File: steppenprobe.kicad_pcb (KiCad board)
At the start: 2 copper layers, 50 x 60 mm, 75 parts, among them J1 USB_C_Receptacle_USB2.0, J2 Conn_01x12, U1 SRV05-4, U2 XC6206PxxxMR, U3 FT2232HL, U4 74LVC1G125, U5 74LVC1G125, U6 74LVC1G125, U7 74LVC1G125, U8 74LVC1G125, U9 74LVC1G125, Y1 Crystal_GND24

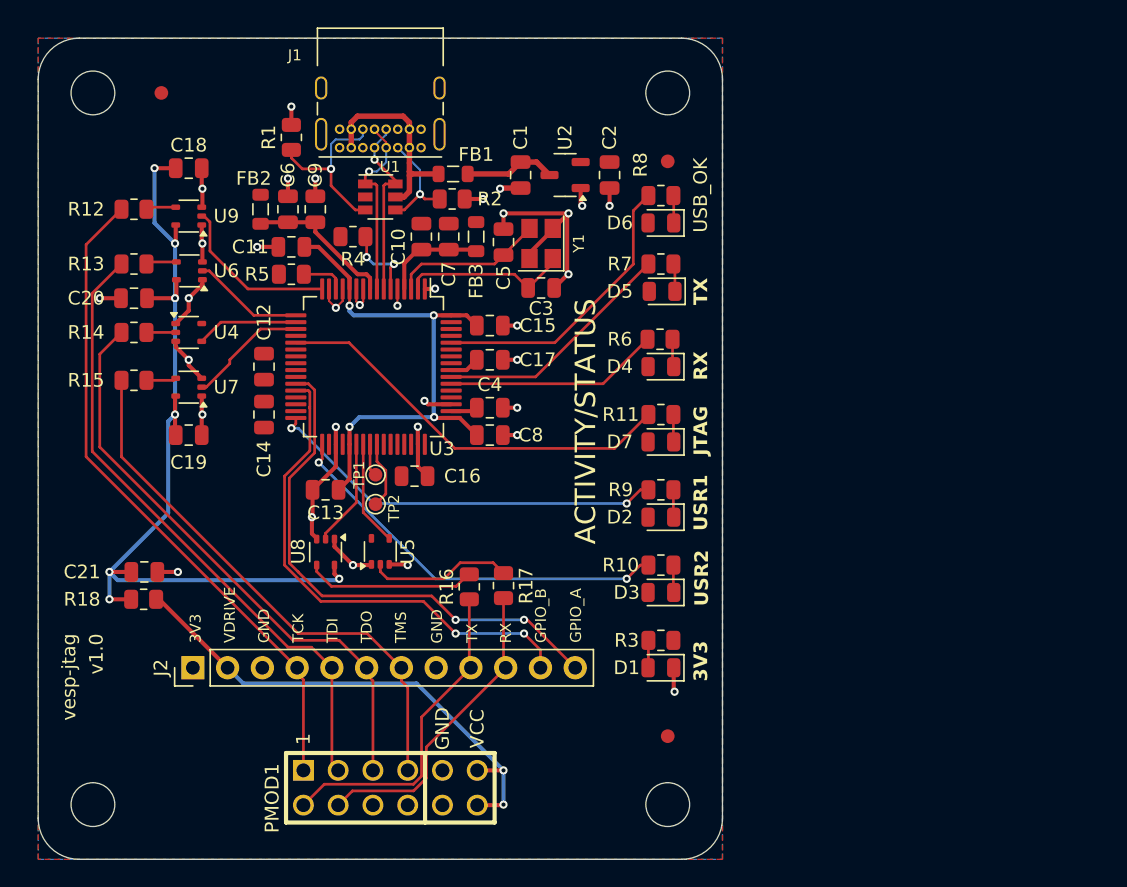
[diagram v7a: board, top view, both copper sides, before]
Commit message: Fixed DRC problems, added logo dir.
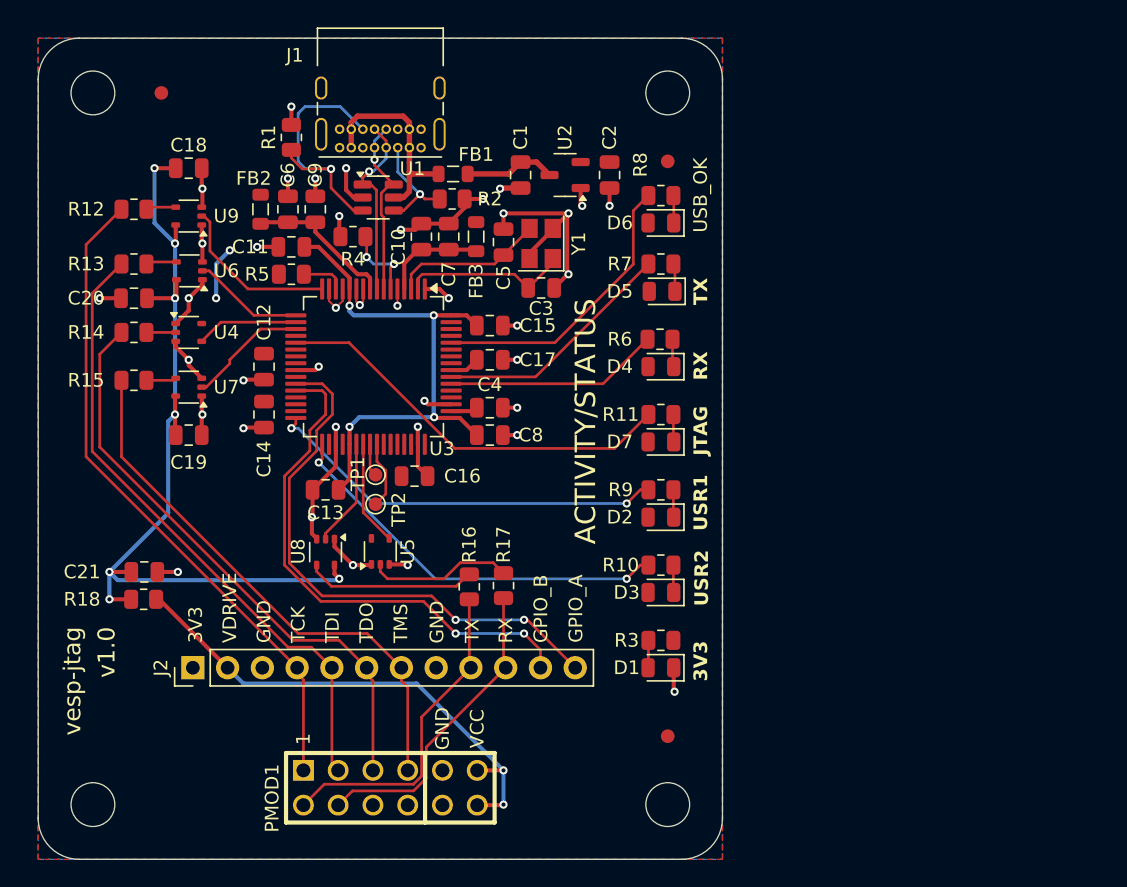
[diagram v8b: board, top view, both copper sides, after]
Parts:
- moved U1 0.16 mm to (124.8, 61.6)
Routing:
- net GND: track 80.4 -> 97.0 mm, vias 33 -> 39
- net /USB_CC2: track 13.2 -> 20.7 mm
- net +3V3: track 4.16 -> 8.08 mm, vias 0 -> 2
- net /GPIO_A: track 39.0 -> 40.7 mm
- net /GPIO_B: track 37.1 -> 38.6 mm
